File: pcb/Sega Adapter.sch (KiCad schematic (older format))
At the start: 6 parts, among them J1 Sega, J2 Atari, J3 ICSP, SW1 C64, U1 PIC16F1847-IP

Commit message: Finished schematic
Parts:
- removed SW1: C64, Button_Switch_THT:SW_E-Switch_EG1224_SPDT_Angled, symbol Switch:SW_SPDT
- added JP1: Prog/C64, Connector_PinHeader_2.54mm:PinHeader_1x03_P2.54mm_Vertical, symbol Device:Jumper_NC_Dual
- J1: footprint Connector_Dsub:DSUB-9_Female_Horizontal_P2.77x2.84mm_EdgePinOffset4.94mm_Housed_MountingHolesOffset7.48mm -> Connector_Dsub:DSUB-9_Male_Horizontal_P2.77x2.84mm_EdgePinOffset7.70mm_Housed_MountingHolesOffset9.12mm
- J2: footprint Connector_Dsub:DSUB-9_Male_Horizontal_P2.77x2.84mm_EdgePinOffset4.94mm_Housed_MountingHolesOffset7.48mm -> Connector_Dsub:DSUB-9_Female_Horizontal_P2.77x2.84mm_EdgePinOffset7.70mm_Housed_MountingHolesOffset9.12mm
- J3: footprint Connector_PinHeader_2.54mm:PinHeader_1x06_P2.54mm_Horizontal -> Connector_PinHeader_2.54mm:PinHeader_1x06_P2.54mm_Vertical
- U1: value PIC16F1847-IP -> PIC16F1847
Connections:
- net GND: now reaches C1.1, J1.8, J2.8, J3.3 (VSS), U1.5 (VSS)
- net GND: now also J1.0 (PAD), J2.0 (PAD), JP1.3
- net +5V: now reaches C1.2, J1.5, J2.7, J3.2 (VDD), U1.14 (VDD)
- net at U1.4 (~MCLR~/Vpp/RA5): now also JP1.2
- net at J3.1 (~MCLR~/VPP): now also JP1.1
- no-connect marks 0 -> 2
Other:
- moved on the sheet: C1, J3
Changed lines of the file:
@@
 P 7150 3950
 F 0 "U1" H 7150 4831 50  0000 C CNN
-F 1 "PIC16F1847-IP" H 7150 4740 50  0000 C CNN
+F 1 "PIC16F1847" H 7150 4740 50  0000 C CNN
 F 2 "Package_DIP:DIP-18_W7.62mm" H 7150 3950 50  0001 C CIN
 F 3 "http://ww1.microchip.com/downloads/en/DeviceDoc/40300c.pdf" H 7150 3950 50  0001 C CNN
@@
 F 0 "J2" H 9580 3952 50  0000 L CNN
 F 1 "Atari" H 9580 3861 50  0000 L CNN
-F 2 "Connector_Dsub:DSUB-9_Male_Horizontal_P2.77x2.84mm_EdgePinOffset4.94mm_Housed_MountingHolesOffset7.48mm" H 9400 3950 50  0001 C CNN
+F 2 "Connector_Dsub:DSUB-9_Female_Horizontal_P2.77x2.84mm_EdgePinOffset7.70mm_Housed_MountingHolesOffset9.12mm" H 9400 3950 50  0001 C CNN
 F 3 " ~" H 9400 3950 50  0001 C CNN
 	1    9400 3950
@@
 F 0 "J1" H 4729 3809 50  0000 L CNN
 F 1 "Sega" H 4729 3900 50  0000 L CNN
-F 2 "Connector_Dsub:DSUB-9_Female_Horizontal_P2.77x2.84mm_EdgePinOffset4.94mm_Housed_MountingHolesOffset7.48mm" H 4550 3900 50  0001 C CNN
+F 2 "Connector_Dsub:DSUB-9_Male_Horizontal_P2.77x2.84mm_EdgePinOffset7.70mm_Housed_MountingHolesOffset9.12mm" H 4550 3900 50  0001 C CNN
 F 3 " ~" H 4550 3900 50  0001 C CNN
 	1    4550 3900
@@
 L Device:C C1
 U 1 1 601532C7
-P 7200 5400
-F 0 "C1" V 7452 5400 50  0000 C CNN
-F 1 "0.1uF" V 7361 5400 50  0000 C CNN
-F 2 "Capacitor_THT:C_Axial_L3.8mm_D2.6mm_P7.50mm_Horizontal" H 7238 5250 50  0001 C CNN
-F 3 "~" H 7200 5400 50  0001 C CNN
-	1    7200 5400
+P 8200 2800
+F 0 "C1" V 8452 2800 50  0000 C CNN
+F 1 "0.1uF" V 8361 2800 50  0000 C CNN
+F 2 "Capacitor_THT:C_Axial_L3.8mm_D2.6mm_P7.50mm_Horizontal" H 8238 2650 50  0001 C CNN
+F 3 "~" H 8200 2800 50  0001 C CNN
+	1    8200 2800
 	0    -1   -1   0
 $EndComp
 Wire Wire Line
-	7150 4650 7050 4650
-Wire Wire Line
-	7050 4650 7050 5400
-Wire Wire Line
-	7350 3250 7350 5400
-Wire Wire Line
 	8250 3650 8650 3650
 Wire Wire Line
@@
 Wire Wire Line
 	9000 3850 9000 3250
-Wire Wire Line
-	7150 3250 7350 3250
-Connection ~ 7350 3250
-Wire Wire Line
-	7350 3250 9000 3250
 Wire Wire Line
 	9100 4050 9000 4050
@@
 	8250 4050 8300 4050
 Wire Wire Line
-	7800 4900 7150 4900
-Wire Wire Line
 	4850 3500 6050 3500
 Wire Wire Line
@@
 	4950 4000 4950 4650
 Wire Wire Line
-	4950 4650 7050 4650
-Connection ~ 7050 4650
-Wire Wire Line
 	4850 4200 5250 4200
 Wire Wire Line
@@
 Wire Wire Line
 	7150 4650 9000 4650
-$Comp
-L Switch:SW_SPDT SW1
-U 1 1 60298E4C
-P 8000 5000
-F 0 "SW1" H 8000 4675 50  0000 C CNN
-F 1 "C64" H 8000 4766 50  0000 C CNN
-F 2 "Button_Switch_THT:SW_E-Switch_EG1224_SPDT_Angled" H 8000 5000 50  0001 C CNN
-F 3 "~" H 8000 5000 50  0001 C CNN
-	1    8000 5000
-	-1   0    0    1
-$EndComp
-Wire Wire Line
-	7150 4650 7150 4900
+Wire Wire Line
+	7150 4650 7150 4750
 $Comp
 L Connector:Conn_PIC_ICSP_ICD J3
 U 1 1 602A483D
-P 8000 5900
-F 0 "J3" V 7625 5900 50  0000 C CNN
-F 1 "ICSP" V 7534 5900 50  0000 C CNN
-F 2 "Connector_PinHeader_2.54mm:PinHeader_1x06_P2.54mm_Horizontal" H 8050 6050 50  0001 C CNN
-F 3 "http://ww1.microchip.com/downloads/en/devicedoc/30277d.pdf" V 7700 5750 50  0001 C CNN
-	1    8000 5900
+P 5850 5900
+F 0 "J3" V 5475 5900 50  0000 C CNN
+F 1 "ICSP" V 5384 5900 50  0000 C CNN
+F 2 "Connector_PinHeader_2.54mm:PinHeader_1x06_P2.54mm_Vertical" H 5900 6050 50  0001 C CNN
+F 3 "http://ww1.microchip.com/downloads/en/devicedoc/30277d.pdf" V 5550 5750 50  0001 C CNN
+	1    5850 5900
 	0    -1   -1   0
 $EndComp
-Connection ~ 7350 5400
-Connection ~ 7050 5400
-Wire Wire Line
-	8300 5000 8200 5000
 Wire Wire Line
 	8300 4050 8300 5000
-Wire Wire Line
-	7800 5100 7800 5400
-Wire Wire Line
-	7350 6100 7600 6100
-Wire Wire Line
-	7350 5400 7350 6100
-Wire Wire Line
-	7050 6450 8400 6450
-Wire Wire Line
-	8400 6450 8400 6100
-Wire Wire Line
-	7050 5400 7050 6450
-Wire Wire Line
-	8100 5400 8100 5200
-Wire Wire Line
-	8100 5200 5950 5200
-Wire Wire Line
-	5950 5200 5950 4150
 Wire Wire Line
 	5400 4150 5950 4150
@@
 Wire Wire Line
 	5950 4150 6050 4150
-Wire Wire Line
-	8000 5400 8000 5300
-Wire Wire Line
-	8000 5300 5850 5300
-Wire Wire Line
-	5850 5300 5850 4250
 Connection ~ 5850 4250
 Wire Wire Line
 	5850 4250 6050 4250
+$Comp
+L power:GND #PWR0101
+U 1 1 604F18E9
+P 9000 4650
+F 0 "#PWR0101" H 9000 4400 50  0001 C CNN
+F 1 "GND" H 9005 4477 50  0000 C CNN
+F 2 "" H 9000 4650 50  0001 C CNN
+F 3 "" H 9000 4650 50  0001 C CNN
+	1    9000 4650
+	1    0    0    -1
+$EndComp
+Connection ~ 9000 4650
+$Comp
+L power:+5V #PWR0102
+U 1 1 604F23D4
+P 9000 3250
+F 0 "#PWR0102" H 9000 3100 50  0001 C CNN
+F 1 "+5V" H 9015 3423 50  0000 C CNN
+F 2 "" H 9000 3250 50  0001 C CNN
+F 3 "" H 9000 3250 50  0001 C CNN
+	1    9000 3250
+	1    0    0    -1
+$EndComp
+NoConn ~ 6050 3950
+$Comp
+L power:PWR_FLAG #FLG0101
+U 1 1 604FC2E9
+P 9000 3850
+F 0 "#FLG0101" H 9000 3925 50  0001 C CNN
+F 1 "PWR_FLAG" H 9000 4023 50  0000 C CNN
+F 2 "" H 9000 3850 50  0001 C CNN
+F 3 "~" H 9000 3850 50  0001 C CNN
+	1    9000 3850
+	1    0    0    -1
+$EndComp
+Connection ~ 9000 3850
+$Comp
+L power:PWR_FLAG #FLG0102
+U 1 1 604FF2AB
+P 9000 4050
+F 0 "#FLG0102" H 9000 4125 50  0001 C CNN
+F 1 "PWR_FLAG" H 9000 4223 50  0000 C CNN
+F 2 "" H 9000 4050 50  0001 C CNN
+F 3 "~" H 9000 4050 50  0001 C CNN
+	1    9000 4050
+	1    0    0    -1
+$EndComp
+Connection ~ 9000 4050
+Connection ~ 9000 3250
+Wire Wire Line
+	4950 4650 7150 4650
+$Comp
+L power:GND #PWR0103
+U 1 1 605081F1
+P 6250 6100
+F 0 "#PWR0103" H 6250 5850 50  0001 C CNN
+F 1 "GND" H 6255 5927 50  0000 C CNN
+F 2 "" H 6250 6100 50  0001 C CNN
+F 3 "" H 6250 6100 50  0001 C CNN
+	1    6250 6100
+	1    0    0    -1
+$EndComp
+$Comp
+L power:GND #PWR0104
+U 1 1 60508F0B
+P 8050 2800
+F 0 "#PWR0104" H 8050 2550 50  0001 C CNN
+F 1 "GND" H 8055 2627 50  0000 C CNN
+F 2 "" H 8050 2800 50  0001 C CNN
+F 3 "" H 8050 2800 50  0001 C CNN
+	1    8050 2800
+	1    0    0    -1
+$EndComp
+Wire Wire Line
+	7150 3250 9000 3250
+$Comp
+L power:+5V #PWR0105
+U 1 1 6050DD11
+P 5450 6100
+F 0 "#PWR0105" H 5450 5950 50  0001 C CNN
+F 1 "+5V" H 5465 6273 50  0000 C CNN
+F 2 "" H 5450 6100 50  0001 C CNN
+F 3 "" H 5450 6100 50  0001 C CNN
+	1    5450 6100
+	1    0    0    -1
+$EndComp
+$Comp
+L power:+5V #PWR0106
+U 1 1 6050E5D5
+P 8350 2800
+F 0 "#PWR0106" H 8350 2650 50  0001 C CNN
+F 1 "+5V" H 8365 2973 50  0000 C CNN
+F 2 "" H 8350 2800 50  0001 C CNN
+F 3 "" H 8350 2800 50  0001 C CNN
+	1    8350 2800
+	1    0    0    -1
+$EndComp
+NoConn ~ 6050 5400
+Wire Wire Line
+	5650 5250 5650 5400
+Wire Wire Line
+	5850 4250 5850 5400
+Wire Wire Line
+	5950 4150 5950 5400
+Wire Wire Line
+	5650 5250 7150 5250
+Wire Wire Line
+	7250 5000 8300 5000
+$Comp
+L Device:Jumper_NC_Dual JP1
+U 1 1 604CD86C
+P 7150 5000
+F 0 "JP1" V 7196 5101 50  0000 L CNN
+F 1 "Prog/C64" V 7105 5101 50  0000 L CNN
+F 2 "Connector_PinHeader_2.54mm:PinHeader_1x03_P2.54mm_Vertical" H 7150 5000 50  0001 C CNN
+F 3 "~" H 7150 5000 50  0001 C CNN
+	1    7150 5000
+	0    -1   -1   0
+$EndComp
+$Comp
+L power:GND #PWR0107
+U 1 1 6055DE77
+P 9400 4550
+F 0 "#PWR0107" H 9400 4300 50  0001 C CNN
+F 1 "GND" H 9405 4377 50  0000 C CNN
+F 2 "" H 9400 4550 50  0001 C CNN
+F 3 "" H 9400 4550 50  0001 C CNN
+	1    9400 4550
+	1    0    0    -1
+$EndComp
+$Comp
+L power:GND #PWR0108
+U 1 1 6055E6D2
+P 4550 3300
+F 0 "#PWR0108" H 4550 3050 50  0001 C CNN
+F 1 "GND" H 4555 3127 50  0000 C CNN
+F 2 "" H 4550 3300 50  0001 C CNN
+F 3 "" H 4550 3300 50  0001 C CNN
+	1    4550 3300
+	-1   0    0    1
+$EndComp
 $EndSCHEMATC

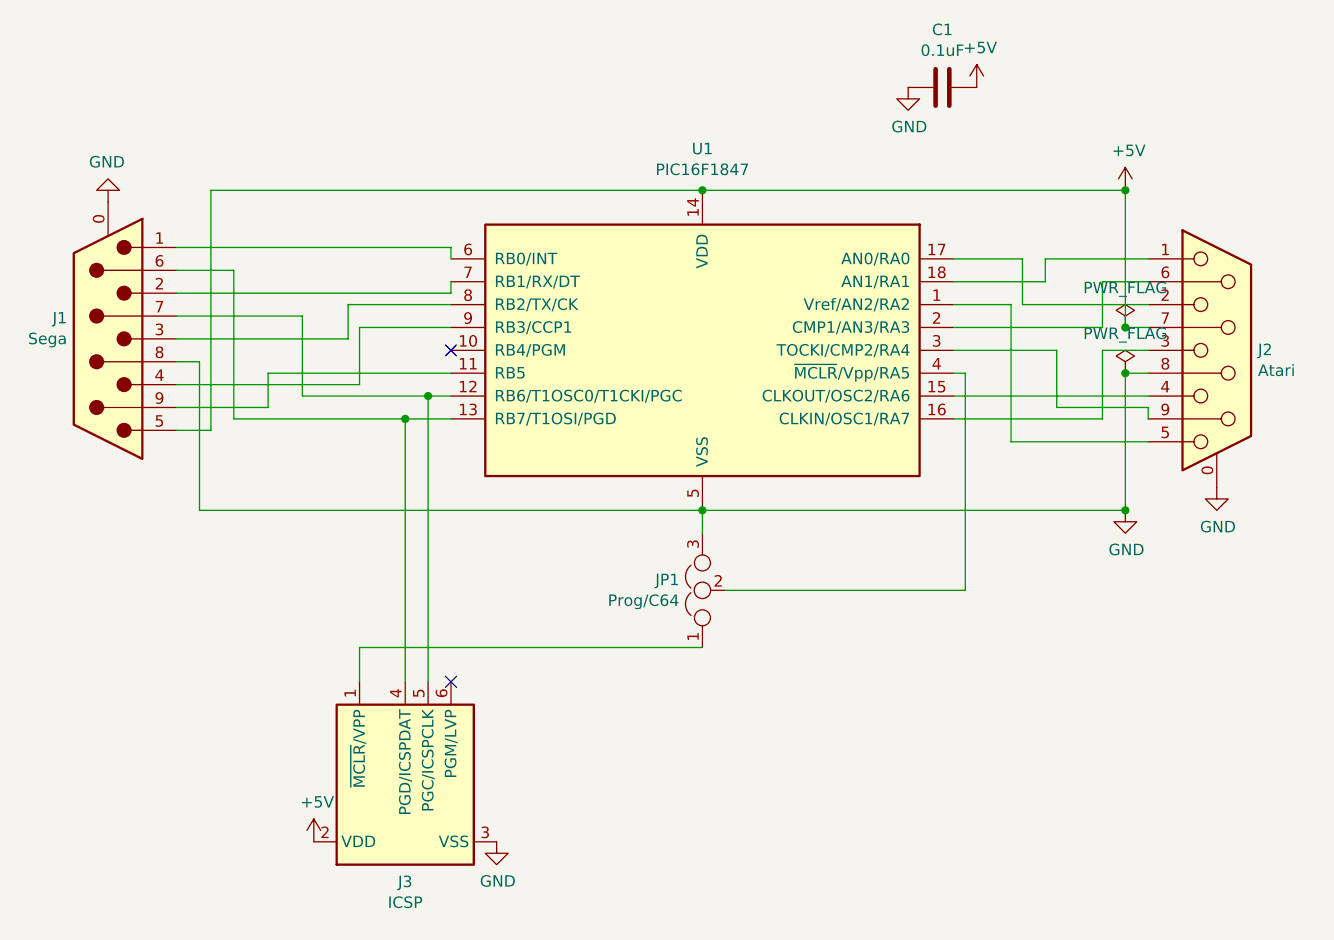
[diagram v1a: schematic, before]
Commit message: More compact PCB
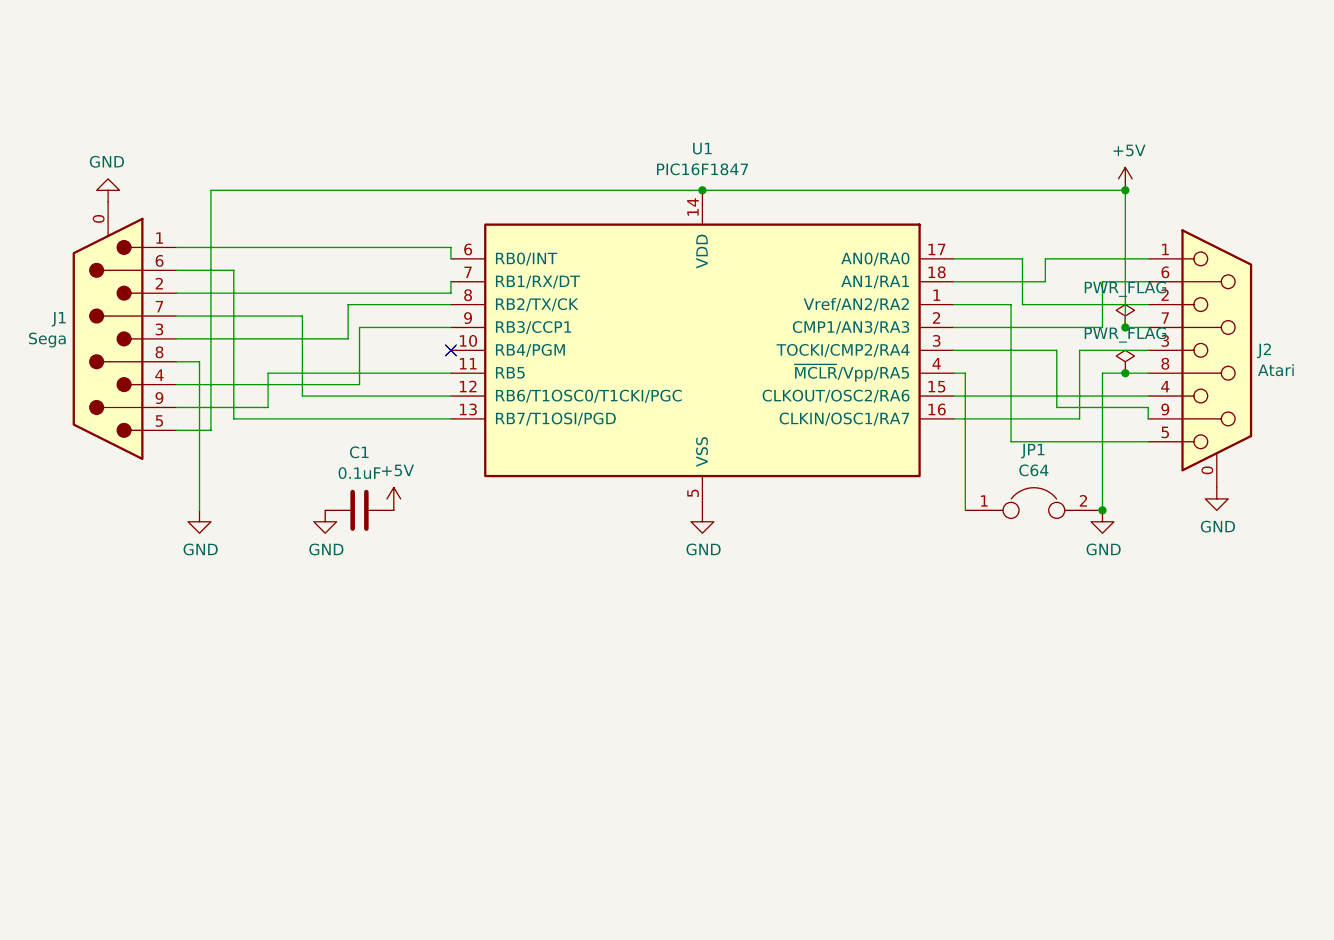
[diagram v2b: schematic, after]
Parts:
- removed J3: ICSP, Connector_PinHeader_2.54mm:PinHeader_1x06_P2.54mm_Vertical, symbol Connector:Conn_PIC_ICSP_ICD
- removed JP1: Prog/C64, Connector_PinHeader_2.54mm:PinHeader_1x03_P2.54mm_Vertical, symbol Device:Jumper_NC_Dual
- added JP1: C64, Connector_PinHeader_2.54mm:PinHeader_1x02_P2.54mm_Vertical, symbol Device:Jumper
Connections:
- net GND: now also JP1.2
- net at U1.4 (~MCLR~/Vpp/RA5): now also JP1.1
- no-connect marks 2 -> 1
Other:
- moved on the sheet: C1
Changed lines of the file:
@@
 Sheet 1 1
 Title "Sega Adapter"
-Date "2021-01-30"
-Rev "1"
+Date "2021-03-15"
+Rev "2"
 Comp ""
 Comment1 ""
@@
 L Device:C C1
 U 1 1 601532C7
-P 8200 2800
-F 0 "C1" V 8452 2800 50  0000 C CNN
-F 1 "0.1uF" V 8361 2800 50  0000 C CNN
-F 2 "Capacitor_THT:C_Axial_L3.8mm_D2.6mm_P7.50mm_Horizontal" H 8238 2650 50  0001 C CNN
-F 3 "~" H 8200 2800 50  0001 C CNN
-	1    8200 2800
+P 5650 4650
+F 0 "C1" V 5902 4650 50  0000 C CNN
+F 1 "0.1uF" V 5811 4650 50  0000 C CNN
+F 2 "Capacitor_THT:C_Axial_L3.8mm_D2.6mm_P7.50mm_Horizontal" H 5688 4500 50  0001 C CNN
+F 3 "~" H 5650 4650 50  0001 C CNN
+	1    5650 4650
 	0    -1   -1   0
 $EndComp
@@
 	8550 3750 9100 3750
 Wire Wire Line
-	8900 4250 8900 3950
-Wire Wire Line
-	8900 3950 9100 3950
-Wire Wire Line
 	8250 4150 9100 4150
 Wire Wire Line
@@
 	8500 3750 8500 4350
 Wire Wire Line
-	8500 4350 9100 4350
-Wire Wire Line
 	8250 3850 8900 3850
 Wire Wire Line
@@
 	8900 3650 9100 3650
 Wire Wire Line
-	8250 4250 8900 4250
+	8250 4250 8800 4250
 Wire Wire Line
 	8250 3950 8700 3950
@@
 Wire Wire Line
 	9100 4050 9000 4050
-Wire Wire Line
-	9000 4050 9000 4650
-Connection ~ 7150 4650
 Wire Wire Line
 	8250 4050 8300 4050
@@
 	5100 3600 5100 4250
 Wire Wire Line
-	5100 4250 5850 4250
-Wire Wire Line
 	4850 3800 5400 3800
 Wire Wire Line
@@
 Wire Wire Line
 	5250 4050 6050 4050
-Wire Wire Line
-	7150 4650 9000 4650
-Wire Wire Line
-	7150 4650 7150 4750
-$Comp
-L Connector:Conn_PIC_ICSP_ICD J3
-U 1 1 602A483D
-P 5850 5900
-F 0 "J3" V 5475 5900 50  0000 C CNN
-F 1 "ICSP" V 5384 5900 50  0000 C CNN
-F 2 "Connector_PinHeader_2.54mm:PinHeader_1x06_P2.54mm_Vertical" H 5900 6050 50  0001 C CNN
-F 3 "http://ww1.microchip.com/downloads/en/devicedoc/30277d.pdf" V 5550 5750 50  0001 C CNN
-	1    5850 5900
-	0    -1   -1   0
-$EndComp
-Wire Wire Line
-	8300 4050 8300 5000
-Wire Wire Line
-	5400 4150 5950 4150
-Connection ~ 5950 4150
-Wire Wire Line
-	5950 4150 6050 4150
-Connection ~ 5850 4250
-Wire Wire Line
-	5850 4250 6050 4250
-$Comp
-L power:GND #PWR0101
-U 1 1 604F18E9
-P 9000 4650
-F 0 "#PWR0101" H 9000 4400 50  0001 C CNN
-F 1 "GND" H 9005 4477 50  0000 C CNN
-F 2 "" H 9000 4650 50  0001 C CNN
-F 3 "" H 9000 4650 50  0001 C CNN
-	1    9000 4650
-	1    0    0    -1
-$EndComp
-Connection ~ 9000 4650
 $Comp
 L power:+5V #PWR0102
@@
 	1    0    0    -1
 $EndComp
-Connection ~ 9000 4050
 Connection ~ 9000 3250
-Wire Wire Line
-	4950 4650 7150 4650
-$Comp
-L power:GND #PWR0103
-U 1 1 605081F1
-P 6250 6100
-F 0 "#PWR0103" H 6250 5850 50  0001 C CNN
-F 1 "GND" H 6255 5927 50  0000 C CNN
-F 2 "" H 6250 6100 50  0001 C CNN
-F 3 "" H 6250 6100 50  0001 C CNN
-	1    6250 6100
-	1    0    0    -1
-$EndComp
 $Comp
 L power:GND #PWR0104
 U 1 1 60508F0B
-P 8050 2800
-F 0 "#PWR0104" H 8050 2550 50  0001 C CNN
-F 1 "GND" H 8055 2627 50  0000 C CNN
-F 2 "" H 8050 2800 50  0001 C CNN
-F 3 "" H 8050 2800 50  0001 C CNN
-	1    8050 2800
+P 5500 4650
+F 0 "#PWR0104" H 5500 4400 50  0001 C CNN
+F 1 "GND" H 5505 4477 50  0000 C CNN
+F 2 "" H 5500 4650 50  0001 C CNN
+F 3 "" H 5500 4650 50  0001 C CNN
+	1    5500 4650
 	1    0    0    -1
 $EndComp
 Wire Wire Line
 	7150 3250 9000 3250
-$Comp
-L power:+5V #PWR0105
-U 1 1 6050DD11
-P 5450 6100
-F 0 "#PWR0105" H 5450 5950 50  0001 C CNN
-F 1 "+5V" H 5465 6273 50  0000 C CNN
-F 2 "" H 5450 6100 50  0001 C CNN
-F 3 "" H 5450 6100 50  0001 C CNN
-	1    5450 6100
-	1    0    0    -1
-$EndComp
 $Comp
 L power:+5V #PWR0106
 U 1 1 6050E5D5
-P 8350 2800
-F 0 "#PWR0106" H 8350 2650 50  0001 C CNN
-F 1 "+5V" H 8365 2973 50  0000 C CNN
-F 2 "" H 8350 2800 50  0001 C CNN
-F 3 "" H 8350 2800 50  0001 C CNN
-	1    8350 2800
-	1    0    0    -1
-$EndComp
-NoConn ~ 6050 5400
-Wire Wire Line
-	5650 5250 5650 5400
-Wire Wire Line
-	5850 4250 5850 5400
-Wire Wire Line
-	5950 4150 5950 5400
-Wire Wire Line
-	5650 5250 7150 5250
-Wire Wire Line
-	7250 5000 8300 5000
-$Comp
-L Device:Jumper_NC_Dual JP1
-U 1 1 604CD86C
-P 7150 5000
-F 0 "JP1" V 7196 5101 50  0000 L CNN
-F 1 "Prog/C64" V 7105 5101 50  0000 L CNN
-F 2 "Connector_PinHeader_2.54mm:PinHeader_1x03_P2.54mm_Vertical" H 7150 5000 50  0001 C CNN
-F 3 "~" H 7150 5000 50  0001 C CNN
-	1    7150 5000
-	0    -1   -1   0
+P 5800 4650
+F 0 "#PWR0106" H 5800 4500 50  0001 C CNN
+F 1 "+5V" H 5815 4823 50  0000 C CNN
+F 2 "" H 5800 4650 50  0001 C CNN
+F 3 "" H 5800 4650 50  0001 C CNN
+	1    5800 4650
+	1    0    0    -1
 $EndComp
 $Comp
@@
 	-1   0    0    1
 $EndComp
+Wire Wire Line
+	5100 4250 6050 4250
+Wire Wire Line
+	5400 4150 6050 4150
+$Comp
+L power:GND #PWR0103
+U 1 1 6050150B
+P 7150 4650
+F 0 "#PWR0103" H 7150 4400 50  0001 C CNN
+F 1 "GND" H 7155 4477 50  0000 C CNN
+F 2 "" H 7150 4650 50  0001 C CNN
+F 3 "" H 7150 4650 50  0001 C CNN
+	1    7150 4650
+	1    0    0    -1
+$EndComp
+$Comp
+L power:GND #PWR0105
+U 1 1 60502096
+P 4950 4650
+F 0 "#PWR0105" H 4950 4400 50  0001 C CNN
+F 1 "GND" H 4955 4477 50  0000 C CNN
+F 2 "" H 4950 4650 50  0001 C CNN
+F 3 "" H 4950 4650 50  0001 C CNN
+	1    4950 4650
+	1    0    0    -1
+$EndComp
+$Comp
+L Device:Jumper JP1
+U 1 1 60502D56
+P 8600 4650
+F 0 "JP1" H 8600 4914 50  0000 C CNN
+F 1 "C64" H 8600 4823 50  0000 C CNN
+F 2 "Connector_PinHeader_2.54mm:PinHeader_1x02_P2.54mm_Vertical" H 8600 4650 50  0001 C CNN
+F 3 "~" H 8600 4650 50  0001 C CNN
+	1    8600 4650
+	1    0    0    -1
+$EndComp
+Wire Wire Line
+	8500 4350 9100 4350
+Wire Wire Line
+	8300 4050 8300 4650
+Wire Wire Line
+	8800 4250 8800 3950
+$Comp
+L power:GND #PWR0101
+U 1 1 604F18E9
+P 8900 4650
+F 0 "#PWR0101" H 8900 4400 50  0001 C CNN
+F 1 "GND" H 8905 4477 50  0000 C CNN
+F 2 "" H 8900 4650 50  0001 C CNN
+F 3 "" H 8900 4650 50  0001 C CNN
+	1    8900 4650
+	1    0    0    -1
+$EndComp
+Wire Wire Line
+	8900 4050 8900 4650
+Wire Wire Line
+	8800 3950 9100 3950
+Connection ~ 8900 4650
+Wire Wire Line
+	8900 4050 9000 4050
+Connection ~ 9000 4050
 $EndSCHEMATC
